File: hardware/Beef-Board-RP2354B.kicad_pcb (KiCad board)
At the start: 2 copper layers, 84 x 59.2 mm, 81 parts, among them J1 USB-C DEVICE, J10 VAUX OUT, J11 B1 LEGACY, J12 B2 LEGACY, J13 B3 LEGACY, J14 B4 LEGACY, J15 B5 LEGACY, J16 B6 LEGACY, J17 B7 LEGACY, J18 B8 LEGACY, J19 B9 LEGACY, J20 B10 LEGACY, J21 B11 LEGACY, J22 USB COMMON, J3 VAUX 5V INPUT, J31 ENCODER 1, J32 ENCODER 2, J33 AE1 0-5V, J34 AE2 0-5V, J4 USB-C AUX POWER, J40 TT RGB, J41 CENTER BAR RGB, J42 UART A 3V3, J43 UART B 3V3, J5 ENC1 A, J6 ENC1 B, J60 BOOTSEL HEADER, J61 BOOTSEL HEADER, J7 ENC2 A, J8 ENC2 B, J9 VAUX OUT, Q1 2N7002, Q10 2N7002, Q11 2N7002, Q2 2N7002, Q3 2N7002, Q4 2N7002, Q5 2N7002, Q6 2N7002, Q7 2N7002, Q8 2N7002, Q9 2N7002, U1 RP2354B, U2 USBLC6-2SC6, U3 AP2112K-3.3, Y1 12MHz CL=10pF

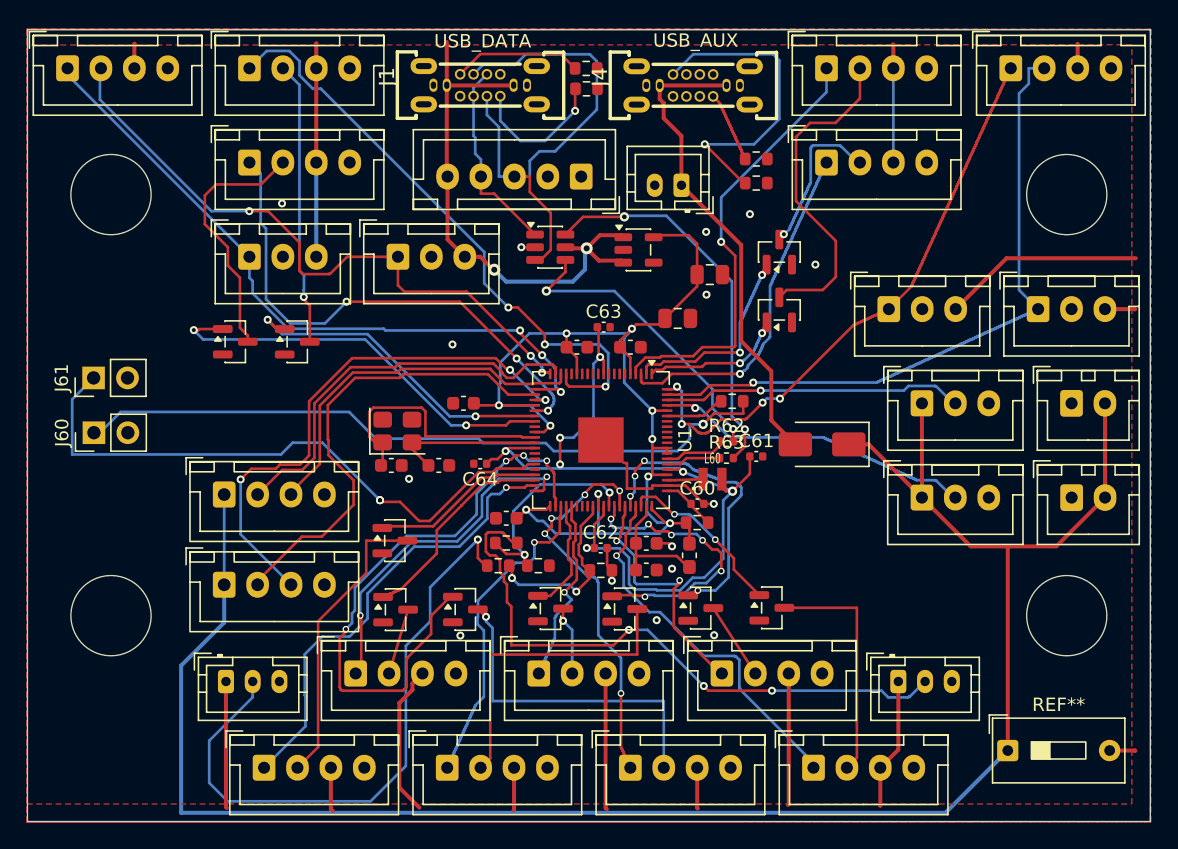
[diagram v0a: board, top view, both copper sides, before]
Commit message: Clean RP2354B routing and ground plane connections
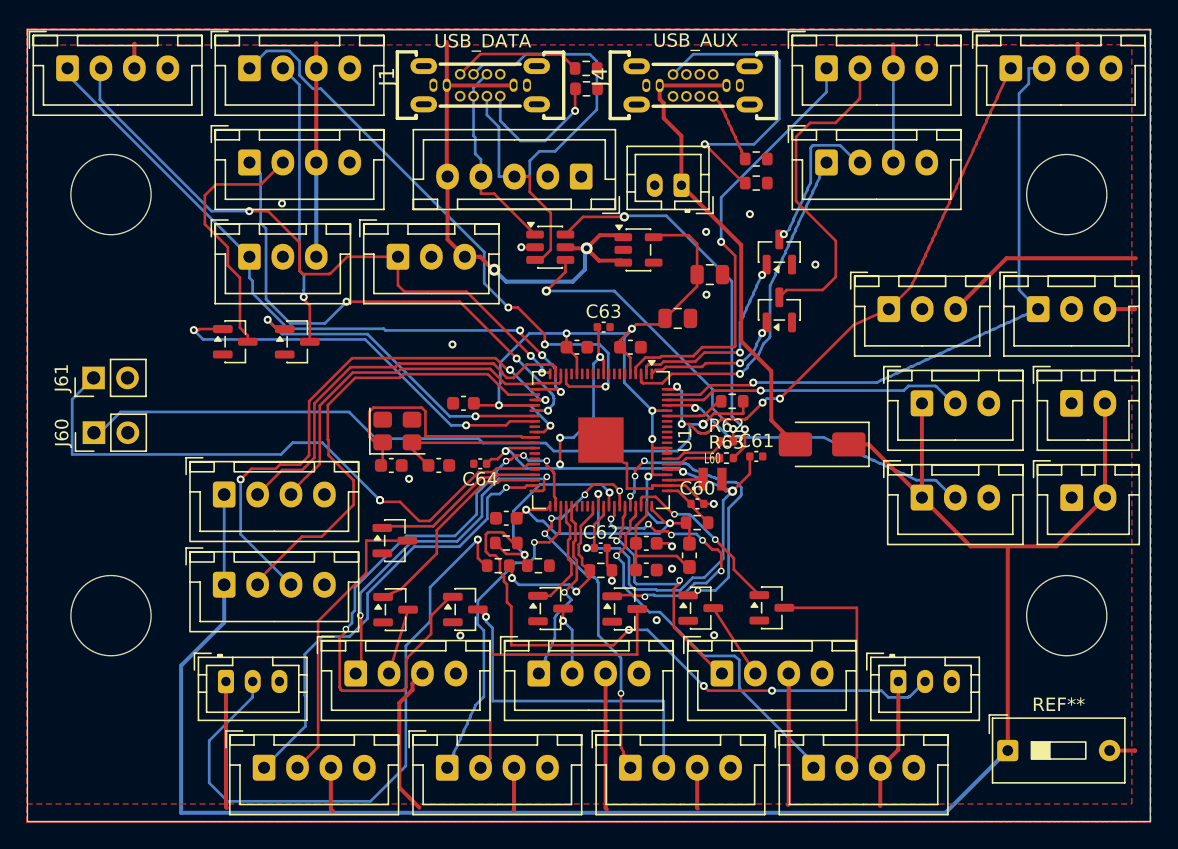
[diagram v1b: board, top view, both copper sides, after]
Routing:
- net /ENC2_A: track 45.5 -> 44.1 mm
- net /ENC2_B: track 50.5 -> 49.6 mm
- net /B9_IN: track 26.9 -> 26.1 mm
- net /CENTER_RGB_3V3: track 24.4 -> 23.8 mm

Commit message: Upload current RP2354B routing optimization
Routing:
- net /ENC2_A: track 44.1 -> 48.0 mm
- net /B3_IN: track 29.5 -> 33.3 mm
- net /ENC1_B: track 48.4 -> 46.7 mm
- net /B8_IN: track 33.1 -> 31.7 mm
- net /USB_D+: track 22.9 -> 24.1 mm
- net /B5_LED_CTL: track 21.4 -> 20.3 mm
- net /USB_CONN_D+: track 38.9 -> 40.0 mm
- net /B5_IN: track 24.4 -> 23.3 mm
- net EXT_5V: track 36.1 -> 37.1 mm
- net /B3_LED_SINK: track 25.1 -> 24.5 mm
- net /+3V3: track 89.8 -> 89.2 mm
- net /B9_LED_CTL: track 15.1 -> 14.5 mm
- net /B10_LED_SINK: track 19.1 -> 18.6 mm
- net /RUN: vias 2 -> 1

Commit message: Set USB-C connector footprints to GT-USB-7038X
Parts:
- J1: footprint Connector_USB:USB_C_Receptacle_GCT_USB4105-xx-A_16P_TopMnt_Horizontal -> BEEF-BOARD:USB-C-TH_G-SWITCH_GT-USB-7038X_1
- J4: footprint Connector_USB:USB_C_Receptacle_G-Switch_GT-USB-7051x -> BEEF-BOARD:USB-C-TH_G-SWITCH_GT-USB-7038X_1
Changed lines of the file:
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@@
 		)
 	)
-	(footprint "Connector_USB:USB_C_Receptacle_G-Switch_GT-USB-7051x"
+	(footprint "BEEF-BOARD:USB-C-TH_G-SWITCH_GT-USB-7038X_1"
 		(layer "F.Cu")
 		(at 132.25 56.145 90)
@@
 		)
 	)
-	(footprint "Connector_USB:USB_C_Receptacle_GCT_USB4105-xx-A_16P_TopMnt_Horizontal"
+	(footprint "BEEF-BOARD:USB-C-TH_G-SWITCH_GT-USB-7038X_1"
 		(layer "F.Cu")
 		(at 116.325 56.13 90)

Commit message: Add power source selector to board and BOM
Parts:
- J61: value BOOTSEL HEADER -> RESET HEADER
- SW1: renamed from REF**; value SW_DIP_SPSTx01_Slide_9.78x4.72mm_W7.62mm_P2.54mm -> POWER SELECT
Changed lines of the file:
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@@
 			)
 		)
-		(property "Value" "BOOTSEL HEADER"
+		(property "Value" "RESET HEADER"
 			(at 0 4.92 90)
 			(layer "F.Fab")
@@
 		(descr "1x-dip-switch SPST , Slide, row spacing 7.62 mm (300 mils), body size 9.78x4.72mm (see e.g. https://www.ctscorp.com/wp-content/uploads/206-208.pdf)")
 		(tags "DIP Switch SPST Slide 7.62mm 300mil")
-		(property "Reference" "REF**"
+		(property "Reference" "SW1"
 			(at 3.81 -3.42 0)
 			(layer "F.SilkS")
@@
 			)
 		)
-		(property "Value" "SW_DIP_SPSTx01_Slide_9.78x4.72mm_W7.62mm_P2.54mm"
+		(property "Value" "POWER SELECT"
 			(at 3.81 3.42 0)
 			(layer "F.Fab")

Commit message: Replace power selector with matched three-pin header
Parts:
- removed SW1: POWER SELECT, Button_Switch_THT:SW_DIP_SPSTx01_Slide_9.78x4.72mm_W7.62mm_P2.54mm
- added J2: POWER SELECT, Connector_PinHeader_2.54mm:PinHeader_1x03_P2.54mm_Vertical, F.Cu at (153.8, 105.9)
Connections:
- D1 pad 1: /VAUX_5V -> /J4_SEL_5V
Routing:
- net /J4_SEL_5V: track 0.00 -> 49.9 mm, vias 0 -> 1
- net /VAUX_5V: track 142.2 -> 137.7 mm
- net /VBUS_5V: track 149.7 -> 153.9 mm
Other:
- board text added: "1"
- board text added: "2"
- board text added: "3"

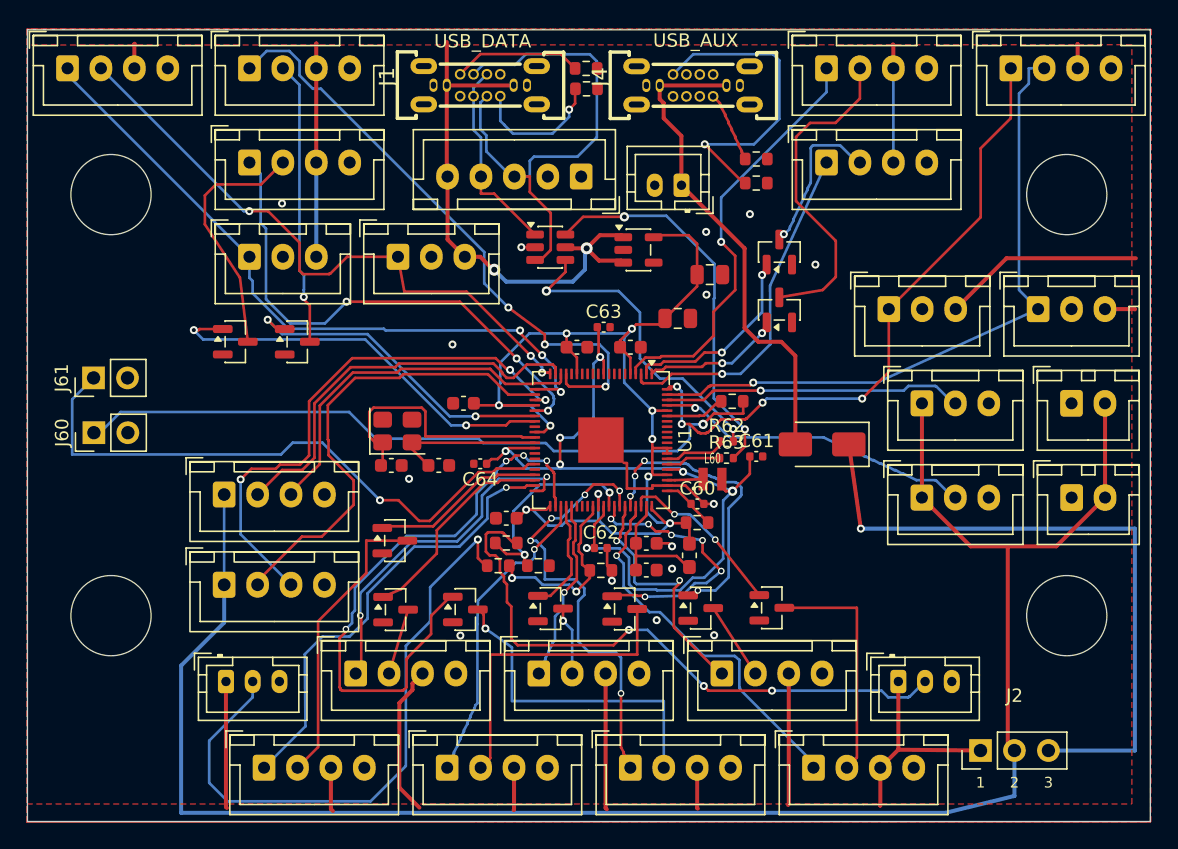
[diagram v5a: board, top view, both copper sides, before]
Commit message: Align schematic BOM and flashing guides with current PCB
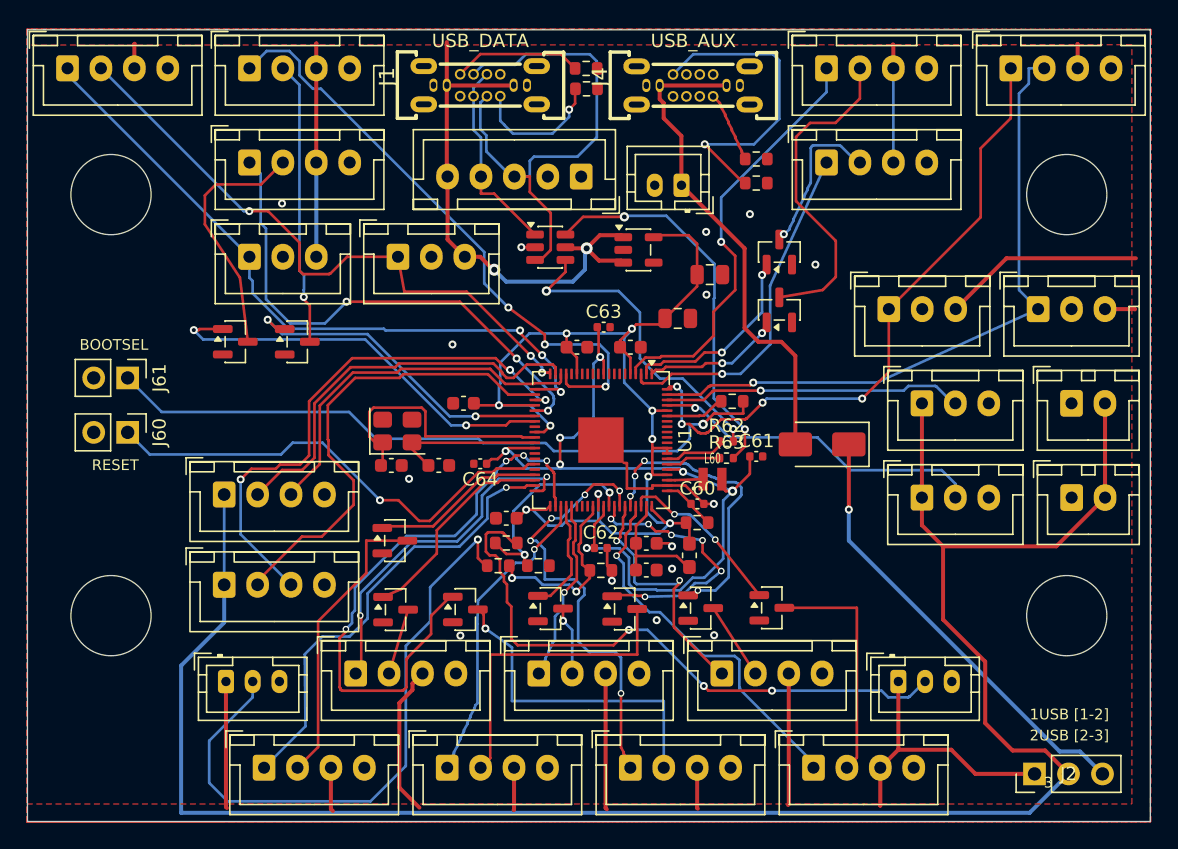
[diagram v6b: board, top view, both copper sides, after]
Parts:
- J60: value BOOTSEL HEADER -> RESET HEADER
- J61: value RESET HEADER -> BOOTSEL HEADER
- moved J2 4.41 mm to (157.8, 107.7)
- moved J61 2.55 mm to (90.0, 78.0), turned to -90 degrees
- moved J60 2.53 mm to (90.0, 82.1), turned to -90 degrees
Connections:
- J60 pad 1: /BOOTSEL_SW -> /RUN
- J61 pad 1: /RUN -> /BOOTSEL_SW
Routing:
- net /J4_SEL_5V: track 49.9 -> 33.4 mm
- net /RUN: track 45.5 -> 35.7 mm
- net /VAUX_5V: track 137.7 -> 147.1 mm
- net /VBUS_5V: track 153.9 -> 158.7 mm
- net /BOOTSEL_SW: track 53.8 -> 51.0 mm
- net /CENTER_RGB_3V3: track 23.8 -> 25.0 mm
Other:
- board text added: "1USB [1-2]"
- board text added: "2USB [2-3]"
- board text added: "BOOTSEL"
- board text added: "RESET"
- board text removed: "1"
- board text removed: "2"

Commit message: Align J3 polarity and docs with revised PCB
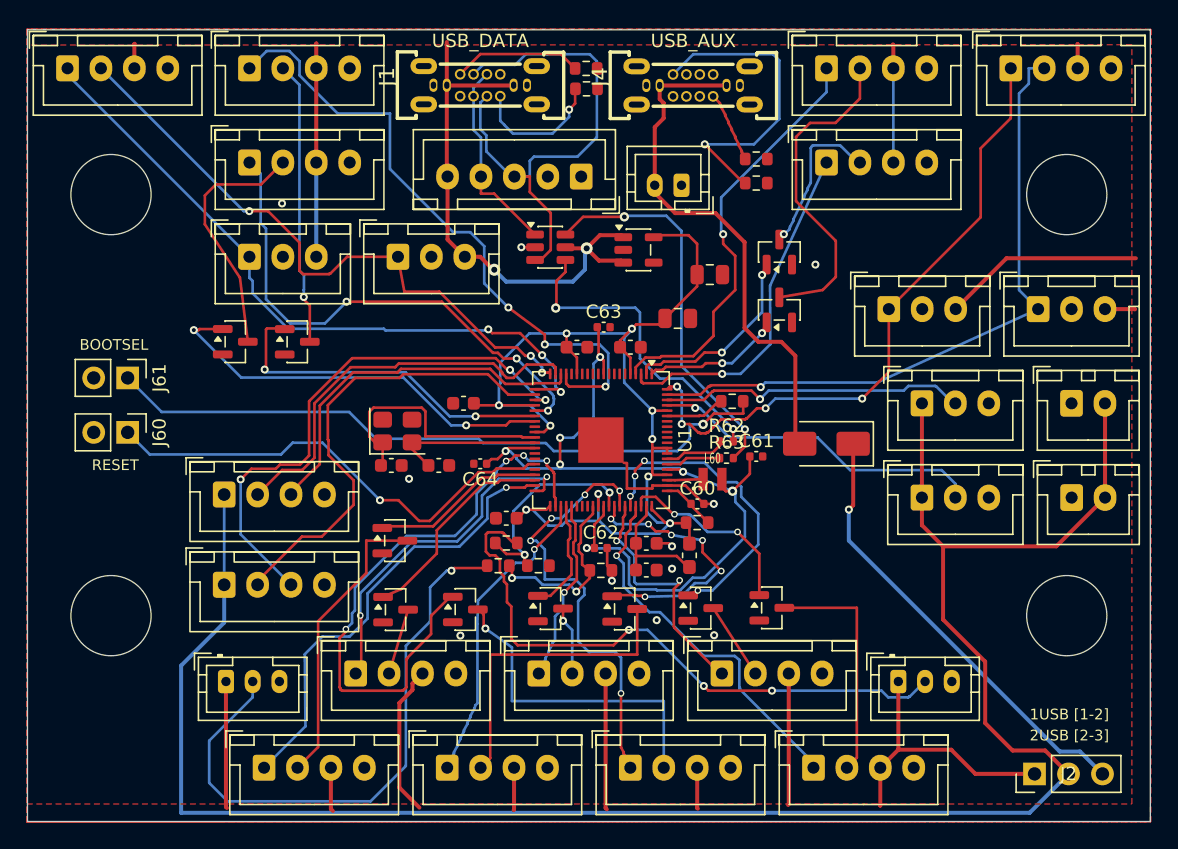
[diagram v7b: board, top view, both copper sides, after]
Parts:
- moved D1 0.33 mm to (142.2, 83.0)
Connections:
- J3 pad 1: EXT_5V -> /GND
- J3 pad 2: /GND -> EXT_5V
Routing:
- net /B11_IN: track 45.3 -> 48.0 mm
- net /AE1_5V_IN: track 47.1 -> 44.6 mm
- net EXT_5V: track 37.1 -> 39.5 mm
- net /B11_LED_CTL: track 24.6 -> 26.2 mm
- net /B1_LED_CTL: track 12.8 -> 14.3 mm
- net /B2_LED_CTL: track 22.4 -> 23.5 mm
- net /+1V1: track 64.8 -> 65.6 mm
- net /TT_RGB_3V3: track 22.5 -> 23.0 mm
- net /GND: track 15.1 -> 15.2 mm, vias 15 -> 11
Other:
- board text removed: "3"

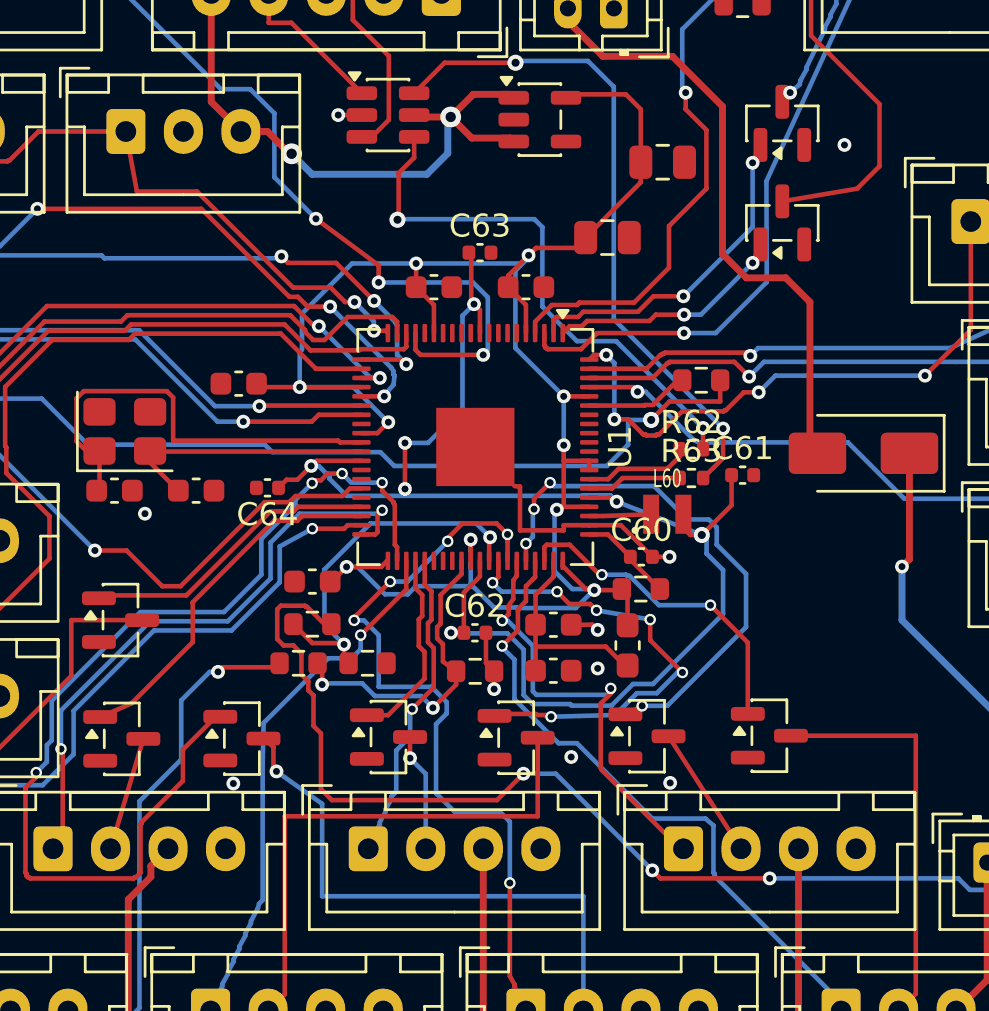
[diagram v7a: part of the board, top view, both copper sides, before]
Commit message: Record revised PCB routing and via count
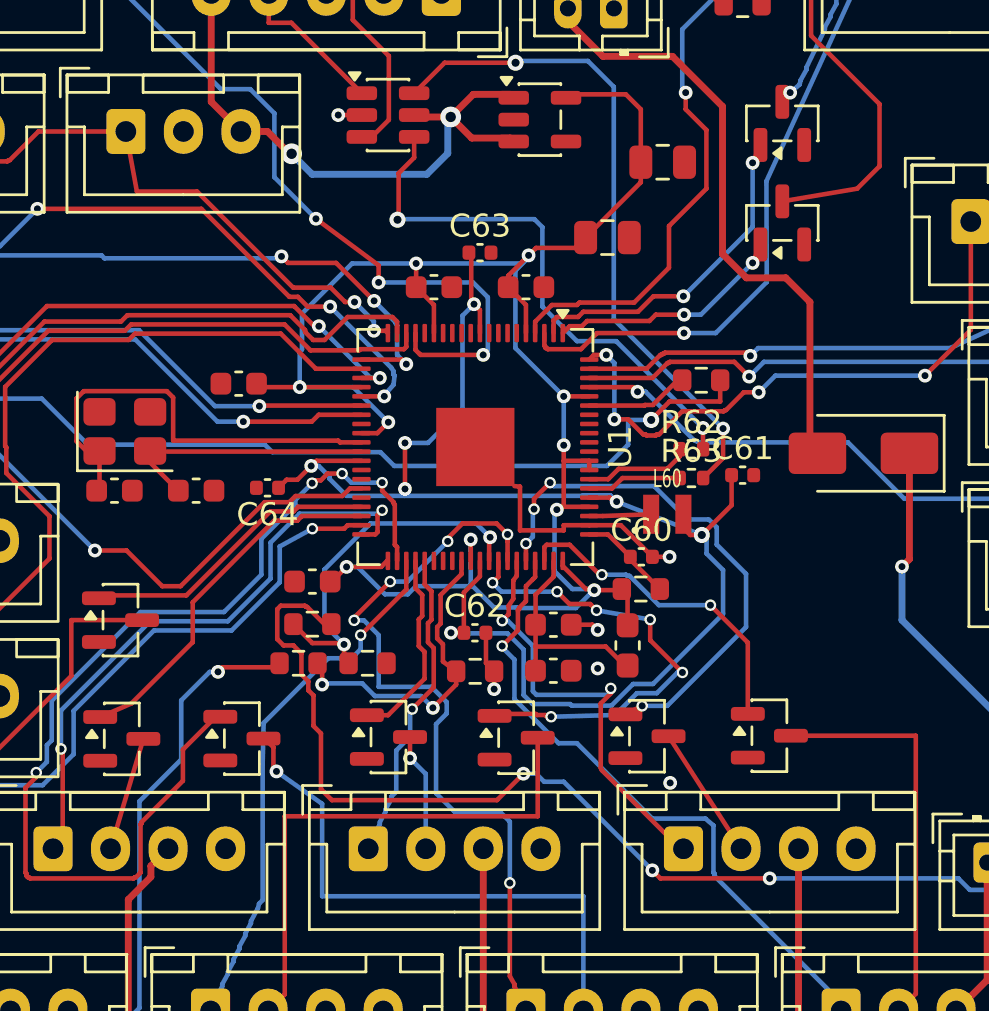
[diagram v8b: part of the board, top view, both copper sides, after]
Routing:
- net /GND: vias 11 -> 7
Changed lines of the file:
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@@
 	)
 	(via
-		(at 114.84 97.302)
-		(size 0.6)
-		(drill 0.3)
-		(layers "F.Cu" "B.Cu")
-		(net "/GND")
-	)
-	(via
 		(at 119.4 68.25)
 		(size 0.6)
@@
 	)
 	(via
-		(at 129.525 96.15)
-		(size 0.6)
-		(drill 0.3)
-		(layers "F.Cu" "B.Cu")
-		(net "/GND")
-	)
-	(via
 		(at 133.825 97.275)
 		(size 0.6)
@@
 	)
 	(via
-		(at 141.4 69.55)
-		(size 0.6)
-		(drill 0.3)
-		(layers "F.Cu" "B.Cu")
-		(net "/GND")
-	)
-	(via
 		(at 130.675 92.3)
 		(size 0.6)
@@
 	)
 	(via
-		(at 111 85.575)
-		(size 0.6)
-		(drill 0.3)
-		(layers "F.Cu" "B.Cu")
-		(net "/GND")
-	)
-	(via
 		(at 133.8 87.45)
 		(size 0.6)
@@
 	)
 	(segment
+		(start 128 96.875)
+		(end 128.35 97.225)
+		(width 0.2)
+		(layer "B.Cu")
+		(net "/AE2_5V_IN")
+	)
+	(segment
 		(start 148.35 101.925)
 		(end 148.4 101.875)
@@
 	)
 	(segment
-		(start 128.85 96.875)
-		(end 133.05 101.075)
+		(start 148.4 101.875)
+		(end 148.45 101.875)
 		(width 0.2)
 		(layer "B.Cu")
@@
 	)
 	(segment
-		(start 148.4 101.875)
-		(end 148.45 101.875)
+		(start 149.6 100.725)
+		(end 149.604 100.738)
 		(width 0.2)
 		(layer "B.Cu")
@@
 	)
 	(segment
-		(start 149.6 100.725)
-		(end 149.604 100.738)
+		(start 129.2 97.225)
+		(end 133.05 101.075)
 		(width 0.2)
 		(layer "B.Cu")
@@
 	)
 	(segment
-		(start 127.45 96.875)
-		(end 128.85 96.875)
+		(start 128.35 97.225)
+		(end 129.2 97.225)
 		(width 0.2)
 		(layer "B.Cu")
@@
 		(width 0.2)
 		(layer "B.Cu")
+		(net "/AE2_5V_IN")
+	)
+	(segment
+		(start 127.45 96.875)
+		(end 128 96.875)
+		(width 0.2)
+		(layer "B.Cu")
